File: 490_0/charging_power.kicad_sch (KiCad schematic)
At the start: 52 parts, among them J19 B3B-XH-A, SW9 B3F-1000, U7 TPS54531DDA, U8 MP2639AGR-Z

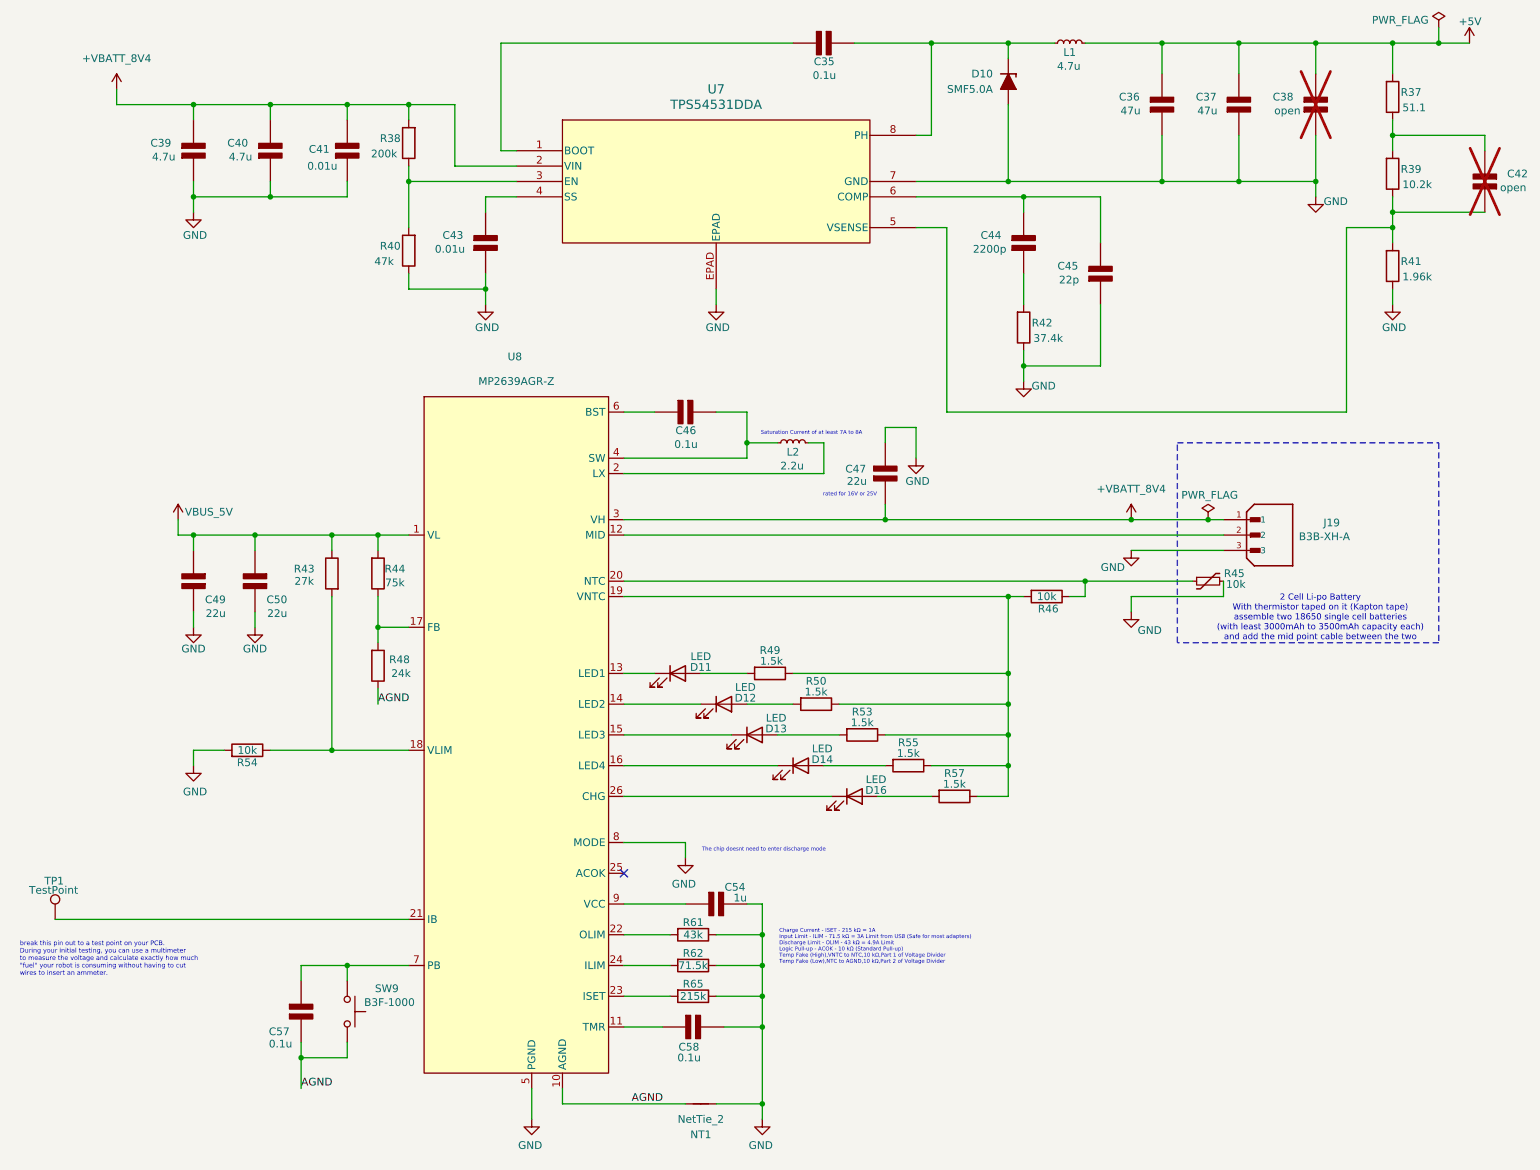
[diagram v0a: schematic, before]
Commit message: Changed buck converter chip
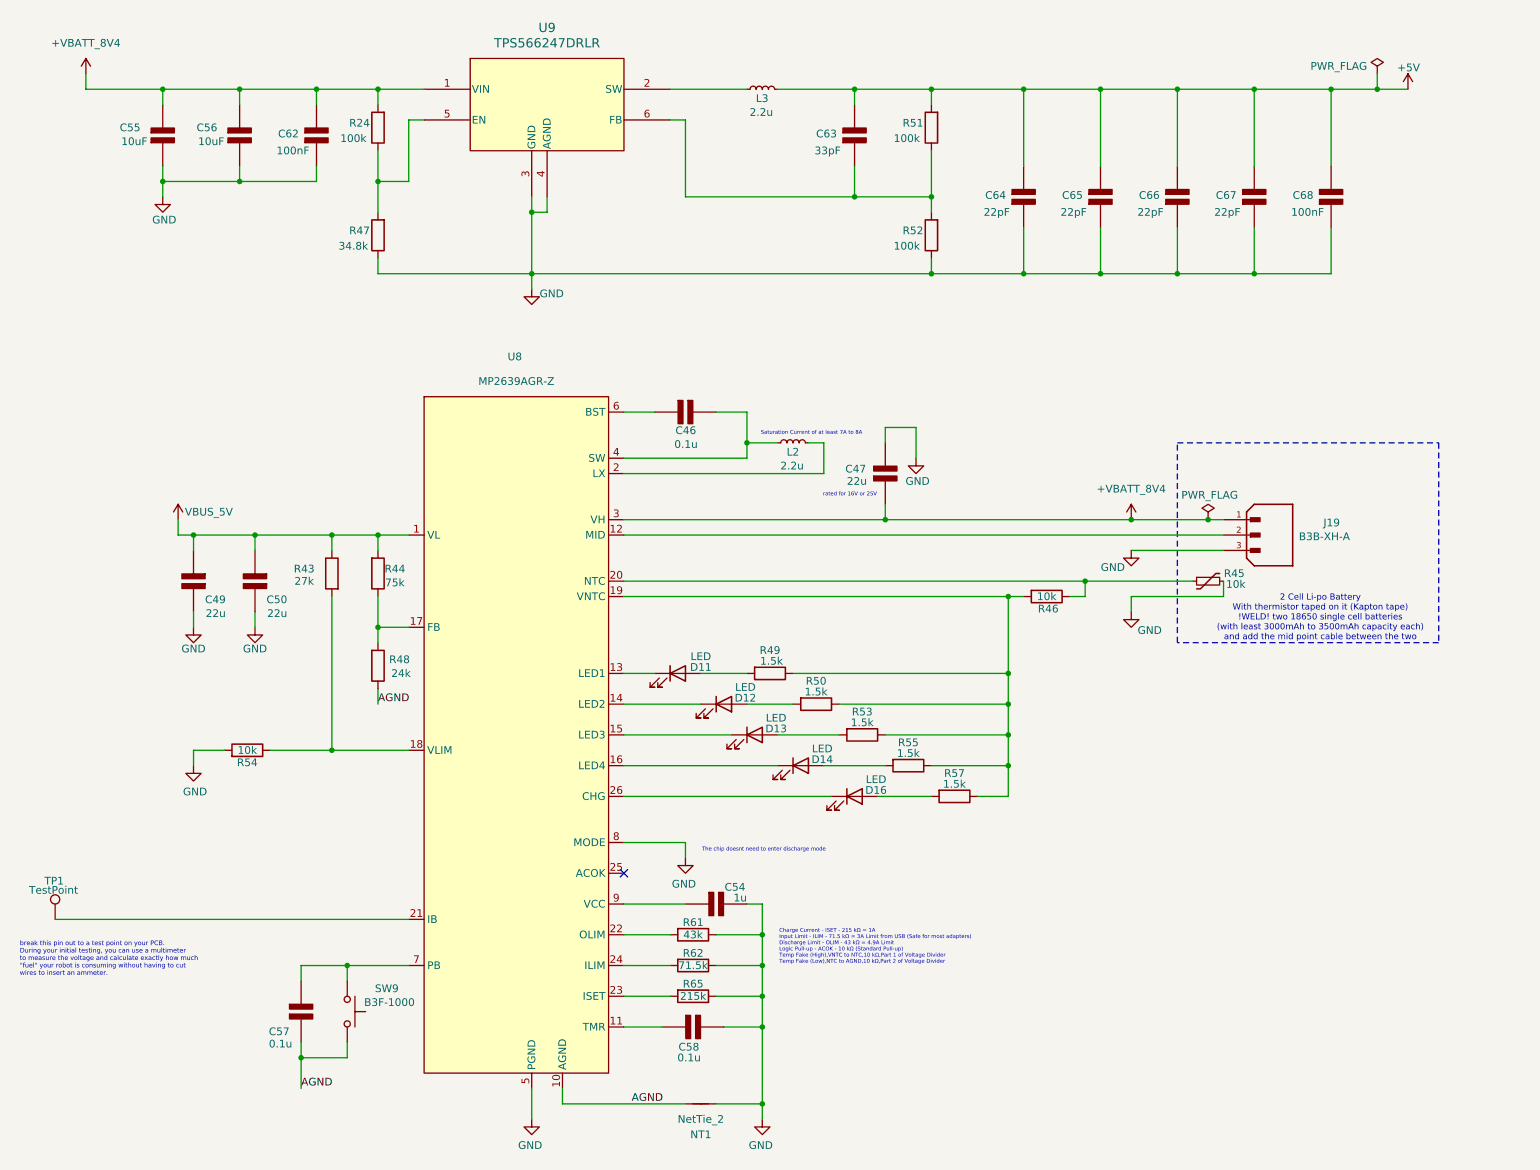
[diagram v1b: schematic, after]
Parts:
- removed C35: 0.1u, symbol PCM_Elektuur:C
- removed C36, C37: 47u, symbol PCM_Elektuur:C
- removed C38, C42: open, symbol PCM_Elektuur:C
- removed C39, C40: 4.7u, symbol PCM_Elektuur:C
- removed C41, C43: 0.01u, symbol PCM_Elektuur:C
- removed C44: 2200p, symbol PCM_Elektuur:C
- removed C45: 22p, symbol PCM_Elektuur:C
- removed D10: SMF5.0A, symbol PCM_Diode_TVS_AKL:SMF5.0A
- removed L1: 4.7u, symbol PCM_SparkFun-Coil:2.2uH_0806_1.2A
- removed R37: 51.1, symbol Device:R
- removed R38: 200k, symbol Device:R
- removed R39: 10.2k, symbol Device:R
- removed R40: 47k, symbol Device:R
- removed R41: 1.96k, symbol Device:R
- removed R42: 37.4k, symbol Device:R
- removed U7: TPS54531DDA, symbol capstone_parts:TPS54531DDA
- added C55, C56: 10uF, symbol PCM_Elektuur:C
- added C62, C68: 100nF, symbol PCM_Elektuur:C
- added C63: 33pF, symbol PCM_Elektuur:C
- added C64, C65, C66, C67: 22pF, symbol PCM_Elektuur:C
- added L3: 2.2u, symbol PCM_SparkFun-Coil:2.2uH_0806_1.2A
- added R24, R51, R52: 100k, symbol Device:R
- added R47: 34.8k, symbol Device:R
- added U9: TPS566247DRLR, SOT-5X3-6_DRL_TEX, symbol capstone_parts:TPS566247DRLR
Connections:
- net +5V: now also C63.2 (-), C64.2 (-), C65.2 (-), C66.2 (-), C67.2 (-), C68.2 (-), L3.2, R51.2
- net +VBATT_8V4: now also C55.2 (-), C56.2 (-), C62.2 (-), R24.2, U9.1 (VIN)
- net GND: now also C55.1 (+), C56.1 (+), C62.1 (+), C64.1 (+), C65.1 (+), C66.1 (+), C67.1 (+), C68.1 (+), R47.1, R52.1, U9.3 (GND), U9.4 (AGND)
- new net: L3.1, U9.2 (SW)
- new net: C63.1 (+), R51.1, R52.2, U9.6 (FB)
- new net: R24.1, R47.2, U9.5 (EN)
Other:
- note added: "2 Cell Li-po Battery With thermistor taped on it (Kapton tape) !WELD! two 18650 single cell batteries (with least 3000mAh to 3500mAh capacity each) and add the mid point cable between the two"
- note removed: "2 Cell Li-po Battery With thermistor taped on it (Kapton tape) assemble two 18650 single cell batteries (with least 3000mAh to 3500mAh capacity each) and add the mid point cable between the two"

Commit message: Updated the schematic
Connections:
- net +VBATT_8V4 renamed +VBATT_7V4
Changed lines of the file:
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@@
 			)
 		)
-		(property "Value" "+VBATT_8V4"
+		(property "Value" "+VBATT_7V4"
 			(at 25.4 17.78 0)
 			(effects
@@
 			)
 		)
-		(property "Value" "+VBATT_8V4"
+		(property "Value" "+VBATT_7V4"
 			(at 198.12 91.44 0)
 			(effects

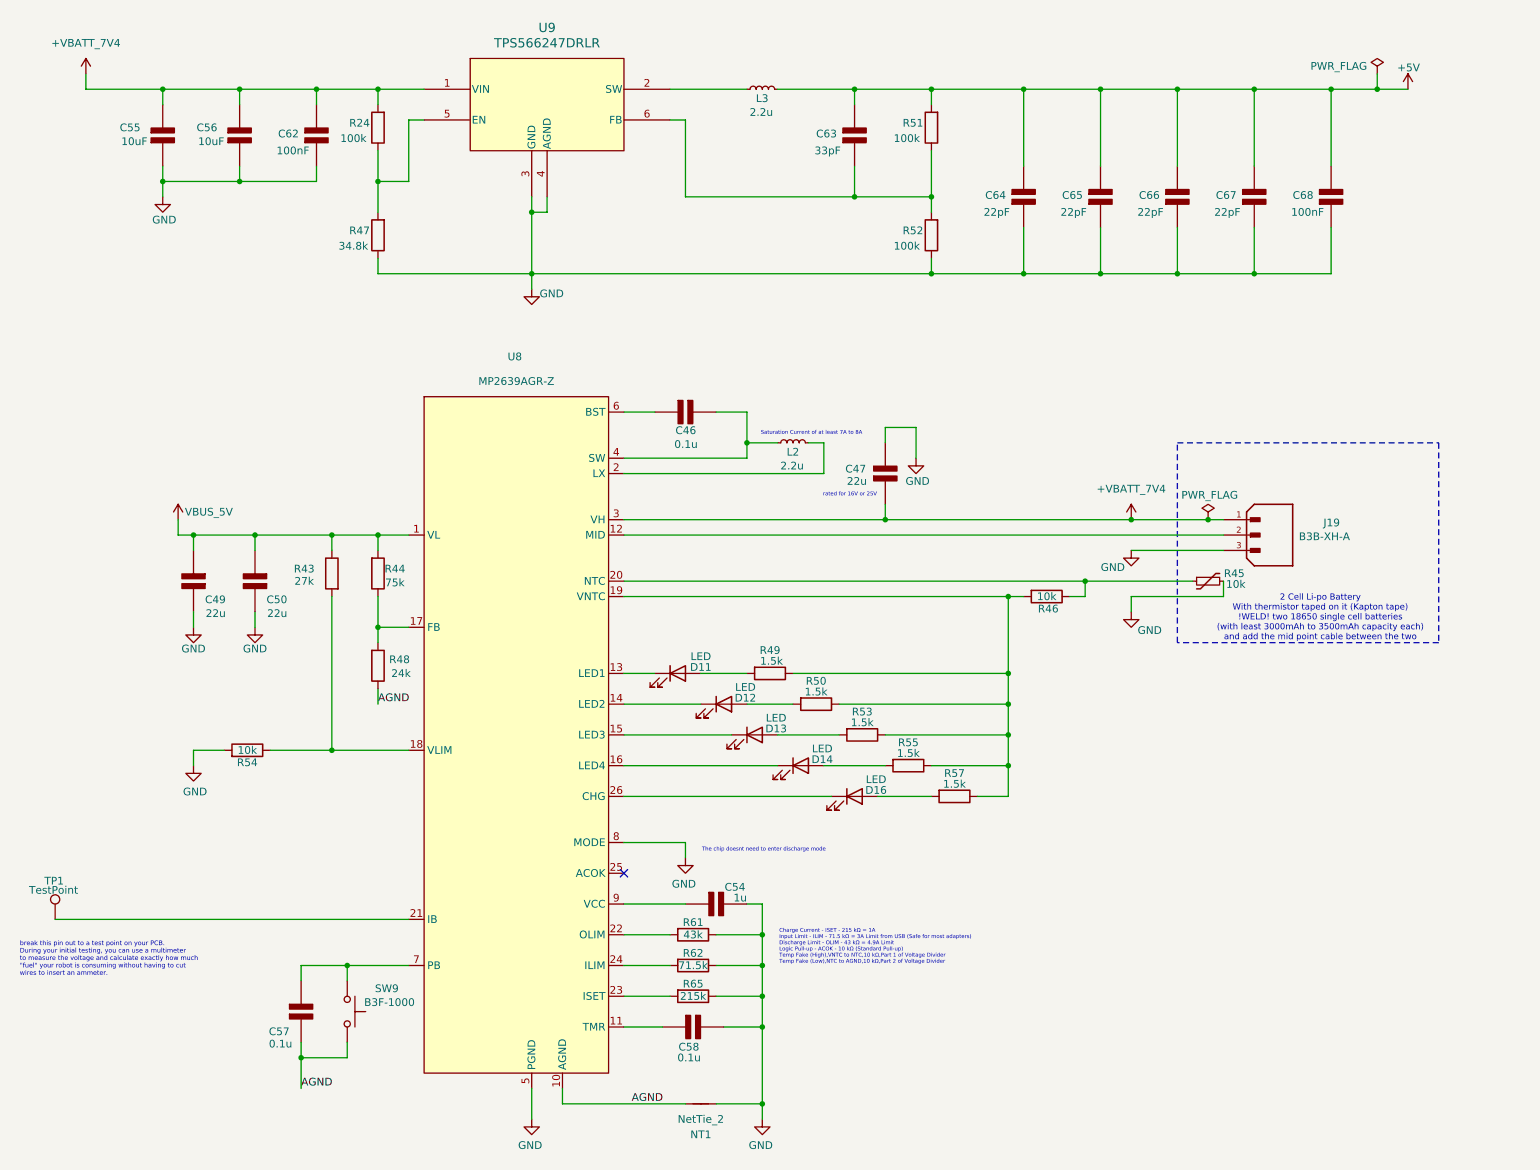
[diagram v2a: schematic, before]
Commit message: Implemented Dmitry comments
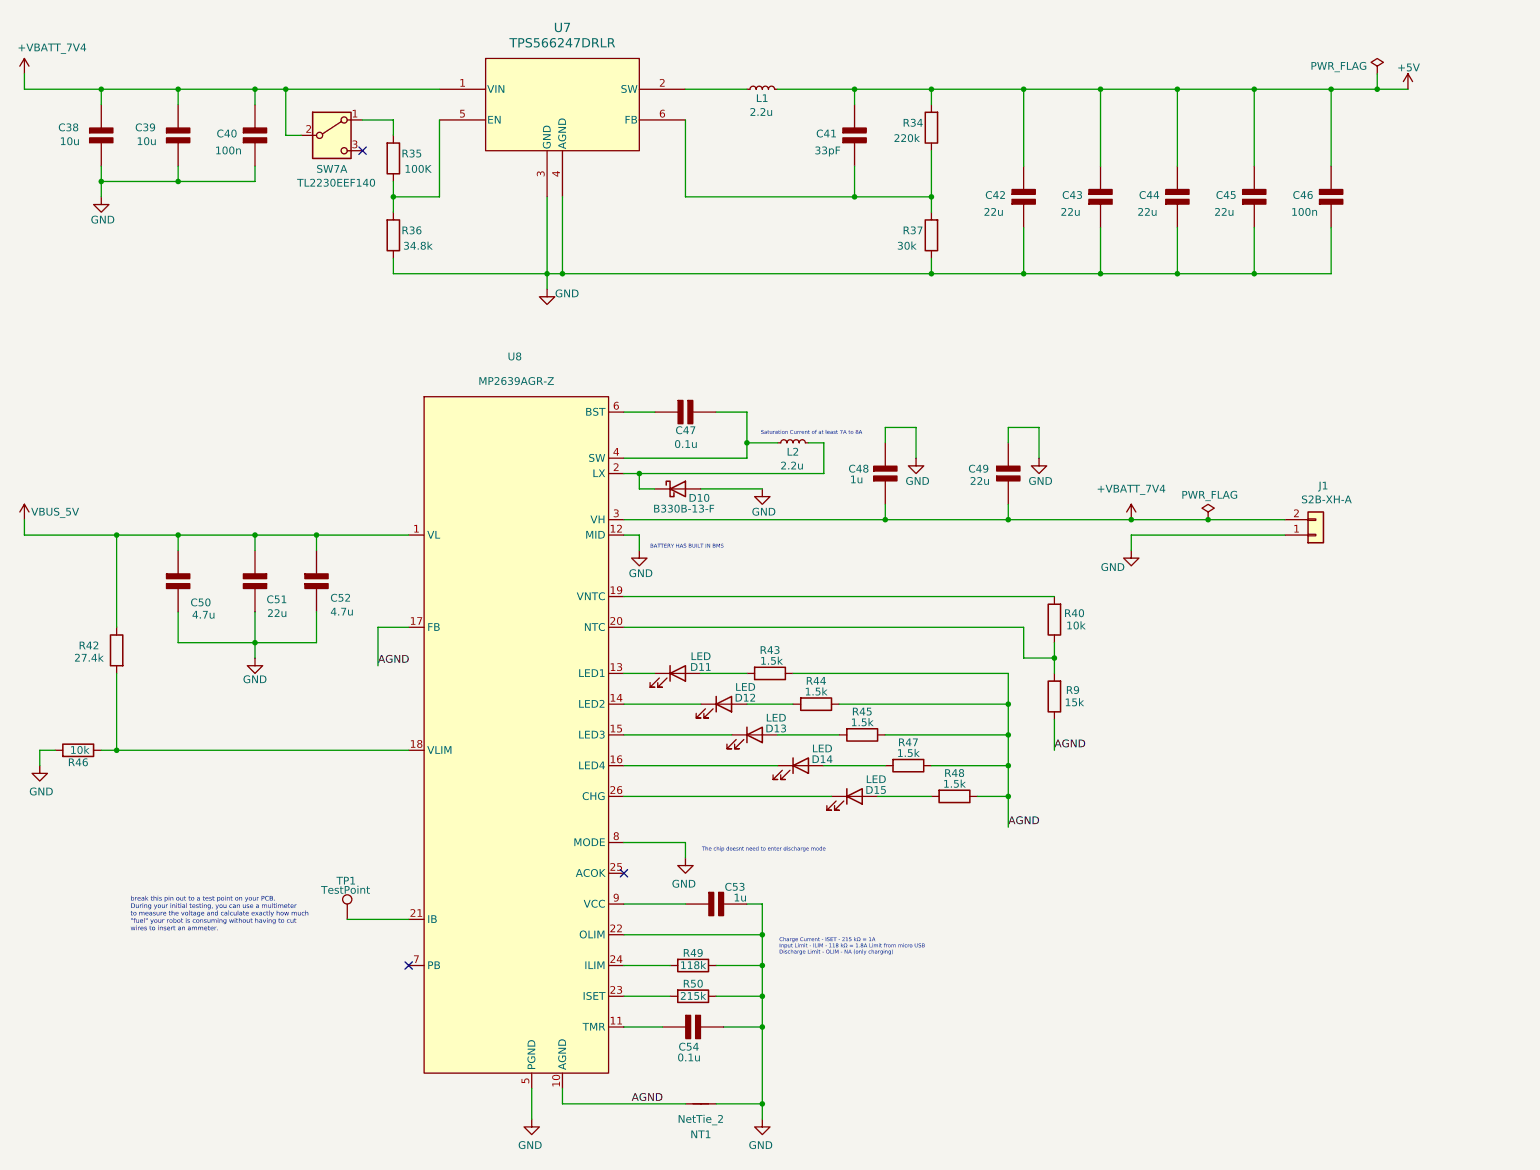
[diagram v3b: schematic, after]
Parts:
- removed C57: 0.1u, symbol PCM_Elektuur:C
- removed J19: B3B-XH-A, B3B-XH-A:JST_B3B-XH-A, symbol capstone_parts:B3B-XH-A
- removed R44: 75k, symbol Device:R
- removed R45: 10k, symbol PCM_SparkFun-Resistor:Thermistor-NTC-10k
- removed R48: 24k, symbol Device:R
- removed R61: 43k, symbol Device:R
- removed SW9: B3F-1000, symbol Switch:SW_Push
- added C48: 1u, symbol PCM_Elektuur:C
- added C52: 4.7u, symbol PCM_Elektuur:C
- added D10: B330B-13-F, Diode_SMD:D_SMA, symbol Diode:MBRA340
- added J1: S2B-XH-A, S2B-XH-A:JST_S2B-XH-A, symbol PCM_4ms_Connector:Conn_01x02
- added R9: 15k, symbol Device:R
- added SW7: TL2230EEF140, symbol Switch:SW_DPDT_x2
- C38: renamed from C55; value 10uF -> 10u; Digikey Link https://www.digikey.ca/en/products/detail/kemet/c1206c475k3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 -> https://www.digikey.ca/en/products/detail/samsung-electro-m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; Manufacturer KEMET -> Samsung Electro-Mechanics; Manufacturer Part C1206C475K3RACTU -> CL31B106KAHNNNE; Price 0.52 -> 0.08; Supplier P/N 399-C1206C475K3RACTUCT-ND -> 1276-1804-1-ND; Type SMD -> SMD, MLCC
- C39: renamed from C56; value 10uF -> 10u; Digikey Link https://www.digikey.ca/en/products/detail/kemet/c1206c475k3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 -> https://www.digikey.ca/en/products/detail/samsung-electro-m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; Manufacturer KEMET -> Samsung Electro-Mechanics; Manufacturer Part C1206C475K3RACTU -> CL31B106KAHNNNE; Price 0.52 -> 0.08; Supplier P/N 399-C1206C475K3RACTUCT-ND -> 1276-1804-1-ND; Type SMD -> SMD, MLCC
- C40: renamed from C62; value 100nF -> 100n; Digikey Link https://www.digikey.ca/en/products/detail/kemet/c1206c103k5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 -> https://www.digikey.ca/en/products/detail/yageo/CC0603KRX7R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; Manufacturer KEMET -> YAGEO; Manufacturer Part C1206C103K5RACTU -> CC0603KRX7R9BB104; Package 1206 (3216 Metric) -> 0603 (1608 Metric); Price 0.15 -> 0.08; Supplier P/N 399-C1206C103K5RACTUCT-ND -> 311-1344-1-ND; Type SMD -> SMD, MLCC
- C41: renamed from C63; Digikey Link https://www.digikey.ca/en/products/detail/kemet/c1206c103k5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 -> https://www.digikey.ca/en/products/detail/kemet/c0603c330j5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; Manufacturer Part C1206C103K5RACTU -> 399-C0603C330J5GACTUCT-ND; Package 1206 (3216 Metric) -> 0603; Price 0.15 -> 0.12; Supplier P/N 399-C1206C103K5RACTUCT-ND -> 399-C0603C330J5GACTUCT-ND; Type SMD -> SMD, MLCC
- C42: renamed from C64; value 22pF -> 22u; Digikey Link https://www.digikey.ca/en/products/detail/kemet/c1206c103k5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 -> https://www.digikey.ca/en/products/detail/samsung-electro-m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; Manufacturer KEMET -> Samsung Electro-Mechanics; Manufacturer Part C1206C103K5RACTU -> CL31A226KAHNNNE; Price 0.15 -> 0.08; Supplier P/N 399-C1206C103K5RACTUCT-ND -> 1276-3047-1-ND
- C43: renamed from C65; value 22pF -> 22u; Digikey Link https://www.digikey.ca/en/products/detail/kemet/c1206c103k5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 -> https://www.digikey.ca/en/products/detail/samsung-electro-m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; Manufacturer KEMET -> Samsung Electro-Mechanics; Manufacturer Part C1206C103K5RACTU -> CL31A226KAHNNNE; Price 0.15 -> 0.08; Supplier P/N 399-C1206C103K5RACTUCT-ND -> 1276-3047-1-ND
- C44: renamed from C66; value 22pF -> 22u; Digikey Link https://www.digikey.ca/en/products/detail/kemet/c1206c103k5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 -> https://www.digikey.ca/en/products/detail/samsung-electro-m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; Manufacturer KEMET -> Samsung Electro-Mechanics; Manufacturer Part C1206C103K5RACTU -> CL31A226KAHNNNE; Price 0.15 -> 0.08; Supplier P/N 399-C1206C103K5RACTUCT-ND -> 1276-3047-1-ND
- C45: renamed from C67; value 22pF -> 22u; Digikey Link https://www.digikey.ca/en/products/detail/kemet/c1206c103k5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 -> https://www.digikey.ca/en/products/detail/samsung-electro-m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; Manufacturer KEMET -> Samsung Electro-Mechanics; Manufacturer Part C1206C103K5RACTU -> CL31A226KAHNNNE; Price 0.15 -> 0.08; Supplier P/N 399-C1206C103K5RACTUCT-ND -> 1276-3047-1-ND
- C46: renamed from C68; value 100nF -> 100n; Digikey Link https://www.digikey.ca/en/products/detail/kemet/c1206c103k5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 -> https://www.digikey.ca/en/products/detail/kemet/C0805C104K5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; Manufacturer Part C1206C103K5RACTU -> C0805C104K5RACTU; Package 1206 (3216 Metric) -> 0805; Price 0.15 -> 0.08; Supplier P/N 399-C1206C103K5RACTUCT-ND -> 399-C0805C104K5RACTUCT-ND; Type SMD -> SMD, MLCC
- C50: value 22u -> 4.7u; Digikey Link https://www.digikey.ca/en/products/detail/samsung-electro-m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 -> https://www.digikey.ca/en/products/detail/kemet/c1206c475k8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; Manufacturer Samsung Electro-Mechanics -> KEMET; Manufacturer Part CL31B226KPHNNNE -> C1206C475K8RACTU; Price 0.39 -> 0.51; Supplier P/N 1276-2769-1-ND -> 399-C1206C475K8RACTUCT-ND
- C53: renamed from C54; Digikey Link https://www.digikey.ca/en/products/detail/kemet/c1206c105k4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 -> https://www.digikey.ca/en/products/detail/samsung-electro-m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; Manufacturer KEMET -> Samsung Electro-Mechanics; Manufacturer Part C1206C105K4RAC7210 -> CL21B105KAFNNNE; Package 1206 (3216 Metric) -> 0805; Price 0.23 -> 0.08; Supplier P/N 399-C1206C105K4RAC7210CT-ND -> 1276-1066-1-ND
- L1: renamed from L3; Digikey Link https://www.digikey.ca/en/products/detail/bourns-inc/SRP654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 -> https://www.digikey.ca/en/products/detail/bourns-inc/srp654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; Manufacturer Part SRP6540-4R7M -> SRP6540-2R2M; Supplier P/N SRP6540-4R7MCT-ND -> SRP6540-2R2MCT-ND
- R34: renamed from R51; value 100k -> 220k; Digikey Link https://www.digikey.ca/en/products/detail/yageo/RC1206FR-07200KL/728676 -> https://www.digikey.ca/en/products/detail/yageo/RC1206FR-07220KL/728694; Manufacturer Part RC1206FR-07200KL -> RC1206FR-07220KL; Supplier P/N 311-200KFRCT-ND -> 311-220KFRCT-ND
- R35: renamed from R24; value 100k -> 100K; Digikey Link https://www.digikey.ca/en/products/detail/yageo/RC1206FR-07200KL/728676 -> https://www.digikey.ca/en/products/detail/yageo/RC1206FR-07100KL/728492; Manufacturer Part RC1206FR-07200KL -> RC1206FR-07100KL; Supplier P/N 311-200KFRCT-ND -> 311-100KFRCT-ND
- R36: renamed from R47; Digikey Link https://www.digikey.ca/en/products/detail/yageo/RC1206FR-0747KL/728931 -> https://www.digikey.ca/en/products/detail/yageo/RC1206FR-0734K8L/728829; Manufacturer Part RC1206FR-0747KL -> RC1206FR-0734K8L; Supplier P/N 311-47.0KFRCT-ND -> 311-34.8KFRCT-ND
- R37: renamed from R52; value 100k -> 30k; Digikey Link https://www.digikey.ca/en/products/detail/yageo/RC1206FR-07200KL/728676 -> https://www.digikey.ca/en/products/detail/yageo/RC1206FR-0730KL/728799; Manufacturer Part RC1206FR-07200KL -> RC1206FR-0730KL; Supplier P/N 311-200KFRCT-ND -> 311-30.0KFRCT-ND
- R42: renamed from R43; value 27k -> 27.4k; Digikey Link https://www.digikey.ca/en/products/detail/yageo/RC1206FR-07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 -> https://www.digikey.ca/en/products/detail/panasonic-electro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; Manufacturer YAGEO -> Panasonic Electronic Components; Manufacturer Part RC1206FR-0727KL -> ERJ-PB6B2742V; Package 1206 -> 0805; Price 0.1 -> 0.21; Supplier P/N 311-27.0KFRCT-ND -> P20756CT-ND
- R49: renamed from R62; value 71.5k -> 118k; Digikey Link https://www.digikey.ca/en/products/detail/yageo/RC0805FR-07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 -> https://www.digikey.ca/en/products/detail/yageo/RC1206FR-07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; Manufacturer Part RC0805FR-0771K5L -> RC1206FR-07118KL; Package 0805 -> 1206; Supplier P/N 311-71.5KCRCT-ND -> 311-118KFRCT-ND
- U7: renamed from U9; Digikey Link (none) -> https://www.digikey.ca/en/products/detail/texas-instruments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; Manufacturer (none) -> Texas Instruments; Manufacturer Part (none) -> TPS566247DRLR; Package (none) -> SOT-563; Price (none) -> 0.77; Supplier (none) -> DigiKey; Supplier P/N (none) -> 296-TPS566247DRLRCT-ND; Type (none) -> SMD; Unit (none) -> pcs
- renumbered C46 to C47, C47 to C49, C49 to C51, C58 to C54, D16 to D15, R46 to R40, R49 to R43, R50 to R44, R53 to R45, R54 to R46, R55 to R47, R57 to R48, R65 to R50
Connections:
- net +VBATT_7V4: now also C48.1 (+), J1.2 (Pin_2), SW7.2 (B); no longer R35.2
- net AGND: now also R43.1, R44.1, R45.1, R47.1, R48.1, U8.17 (FB), R9.1
- net GND: now also U8.12 (MID), U8.22 (OLIM), C48.2 (-), C52.2 (-), D10.2 (A), J1.1 (Pin_1)
- net VBUS_5V: now also C52.1 (+)
- net at L2.2, U8.2 (LX): now also D10.1 (K)
- net at R40.1, U8.20 (NTC): now also R9.2
- new net: R40.2, U8.19 (VNTC)
- new net: R35.2, SW7.1 (A)
- no-connect marks 1 -> 3
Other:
- note added: "BATTERY HAS BUILT IN BMS"
- note added: "Charge Current - ISET - 215 kΩ = 1A Input Limit - ILIM - 118 kΩ = 1.8A Limit from micro USB Discharge Limit - OLIM - NA (only charging)"
- note removed: "2 Cell Li-po Battery With thermistor taped on it (Kapton tape) !WELD! two 18650 single cell batteries (with least 3000mAh to 3500mAh capacity each) and add the mid point cable between the two"
- note removed: "Charge Current - ISET - 215 kΩ = 1A Input Limit - ILIM - 71.5 kΩ = 3A Limit from USB (Safe for most adapters) Discharge Limit - OLIM - 43 kΩ = 4.9A Limit Logic Pull-up - ACOK - 10 kΩ (Standard Pull-up) Temp Fake (High),VNTC to NTC,10 kΩ,Part 1 of Voltage Divider Temp Fake (Low),NTC to AGND,10 kΩ,Part 2 of Voltage Divider"
- note removed: "rated for 16V or 25V"
- moved on the sheet: C38, C39, C40, C49, C51, R35, R36, R40, R42, R46, TP1, U7
